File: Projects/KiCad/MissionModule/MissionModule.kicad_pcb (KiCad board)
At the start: 2 copper layers, 110 x 95 mm, 26 parts, among them J1 Conn_01x04_Pin, J2 Conn_01x04_Pin, J3 Micro_SD_Card_Det_Hirose_DM3AT, U1 ABX00012, U2 MCP2562-E-P, U3 LT1584-3.3, U4 TLP222A, U5 MCP2515-I/P, Y1 8MHz

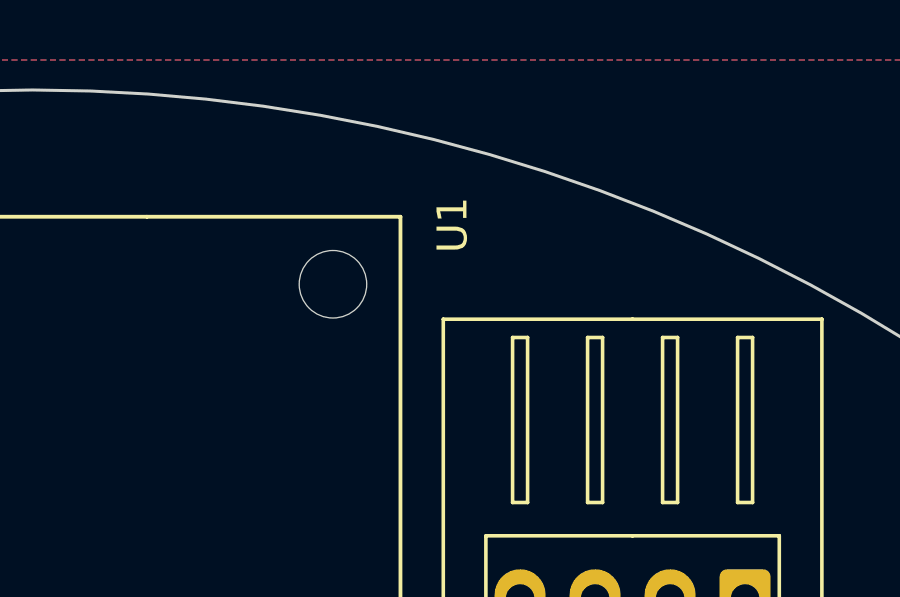
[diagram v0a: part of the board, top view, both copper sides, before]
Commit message: ADXL375のCSをGNDに接続
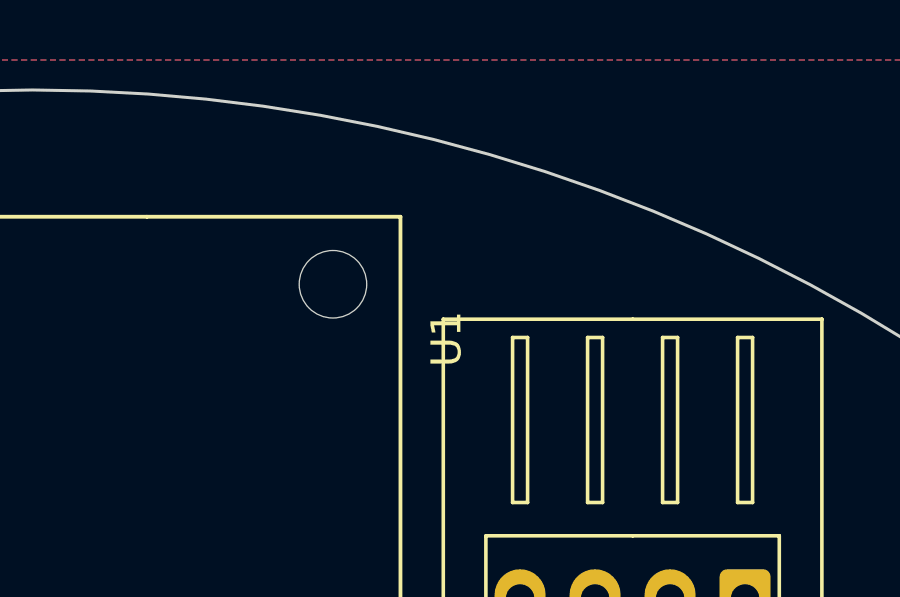
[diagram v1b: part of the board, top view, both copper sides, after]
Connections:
- U6 pad 4: unconnected-(U6-SDO/ALT_ADDRESS-Pad4) -> GND
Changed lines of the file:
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@@
   (net 51 "I2C_SCL")
   (net 52 "I2C_SDA")
-  (net 53 "unconnected-(U6-SDO{slash}ALT_ADDRESS-Pad4)")
-  (net 54 "unconnected-(U6-INT2-Pad6)")
-  (net 55 "unconnected-(U6-INT1-Pad7)")
+  (net 53 "unconnected-(U6-INT2-Pad6)")
+  (net 54 "unconnected-(U6-INT1-Pad7)")
   (footprint "Fuse:Fuse_BelFuse_0ZRE0005FF_L8.3mm_W3.8mm" (layer "F.Cu")
     (at 155.05 133.3 180)
@@
       (net 52 "I2C_SDA") (pinfunction "SDA/SDI/SDIO") (pintype "input"))
     (pad "4" thru_hole circle (at -3.73 9.04 270) (size 1.524 1.524) (drill 0.762) (layers "*.Cu" "*.Mask")
-      (net 53 "unconnected-(U6-SDO{slash}ALT_ADDRESS-Pad4)") (pinfunction "SDO/ALT_ADDRESS") (pintype "output+no_connect"))
+      (net 2 "GND") (pinfunction "SDO/ALT_ADDRESS") (pintype "output"))
     (pad "5" thru_hole circle (at -3.73 11.58 270) (size 1.524 1.524) (drill 0.762) (layers "*.Cu" "*.Mask")
       (net 5 "+3.3V") (pinfunction "~CS") (pintype "input"))
     (pad "6" thru_hole circle (at 3.89 11.58 270) (size 1.524 1.524) (drill 0.762) (layers "*.Cu" "*.Mask")
-      (net 54 "unconnected-(U6-INT2-Pad6)") (pinfunction "INT2") (pintype "output+no_connect"))
+      (net 53 "unconnected-(U6-INT2-Pad6)") (pinfunction "INT2") (pintype "output+no_connect"))
     (pad "7" thru_hole circle (at 3.89 9.04 270) (size 1.524 1.524) (drill 0.762) (layers "*.Cu" "*.Mask")
-      (net 55 "unconnected-(U6-INT1-Pad7)") (pinfunction "INT1") (pintype "output+no_connect"))
+      (net 54 "unconnected-(U6-INT1-Pad7)") (pinfunction "INT1") (pintype "output+no_connect"))
     (pad "8" thru_hole circle (at 3.89 6.5 270) (size 1.524 1.524) (drill 0.762) (layers "*.Cu" "*.Mask")
       (net 2 "GND") (pinfunction "GND") (pintype "power_in"))
@@
     (property "Sheetname" "")
     (attr through_hole)
-    (fp_text reference "U1" (at 0.275 -26.7375 -90) (layer "F.SilkS")
+    (fp_text reference "U1" (at 4.075 -26.535 -90) (layer "F.SilkS")
         (effects (font (size 1 1) (thickness 0.15)))
     )
@@
     (pad "" np_thru_hole circle locked (at 59.25 -2.25 270) (size 2.25 2.25) (drill 2.25) (layers "*.Cu" "*.Mask"))
     (pad "1" thru_hole rect locked (at 22.1348 -2.34 270) (size 1.508 1.508) (drill 1) (layers "*.Cu" "*.Mask")
-      (net 25 "unconnected-(U1-PA03_VREFA{slash}AREF-Pad1)") (pinfunction "PA03_VREFA/AREF") (pintype "bidirectional"))
+      (net 25 "unconnected-(U1-PA03_VREFA{slash}AREF-Pad1)") (pinfunction "PA03_VREFA/AREF") (pintype "bidirectional+no_connect"))
     (pad "2" thru_hole circle locked (at 24.6748 -2.34 270) (size 1.508 1.508) (drill 1) (layers "*.Cu" "*.Mask")
-      (net 26 "unconnected-(U1-PA02_AIN0{slash}DAC0{slash}A0-Pad2)") (pinfunction "PA02_AIN0/DAC0/A0") (pintype "bidirectional"))
+      (net 26 "unconnected-(U1-PA02_AIN0{slash}DAC0{slash}A0-Pad2)") (pinfunction "PA02_AIN0/DAC0/A0") (pintype "bidirectional+no_connect"))
     (pad "3" thru_hole circle locked (at 27.2148 -2.34 270) (size 1.508 1.508) (drill 1) (layers "*.Cu" "*.Mask")
-      (net 27 "unconnected-(U1-PB02_AIN10{slash}A1-Pad3)") (pinfunction "PB02_AIN10/A1") (pintype "bidirectional"))
+      (net 27 "unconnected-(U1-PB02_AIN10{slash}A1-Pad3)") (pinfunction "PB02_AIN10/A1") (pintype "bidirectional+no_connect"))
     (pad "4" thru_hole circle locked (at 29.7548 -2.34 270) (size 1.508 1.508) (drill 1) (layers "*.Cu" "*.Mask")
-      (net 28 "unconnected-(U1-PB03_AIN11{slash}A2-Pad4)") (pinfunction "PB03_AIN11/A2") (pintype "bidirectional"))
+      (net 28 "unconnected-(U1-PB03_AIN11{slash}A2-Pad4)") (pinfunction "PB03_AIN11/A2") (pintype "bidirectional+no_connect"))
     (pad "5" thru_hole circle locked (at 32.2948 -2.34 270) (size 1.508 1.508) (drill 1) (layers "*.Cu" "*.Mask")
-      (net 29 "unconnected-(U1-PA04_AIN4{slash}A3-Pad5)") (pinfunction "PA04_AIN4/A3") (pintype "bidirectional"))
+      (net 29 "unconnected-(U1-PA04_AIN4{slash}A3-Pad5)") (pinfunction "PA04_AIN4/A3") (pintype "bidirectional+no_connect"))
     (pad "6" thru_hole circle locked (at 34.8348 -2.34 270) (size 1.508 1.508) (drill 1) (layers "*.Cu" "*.Mask")
-      (net 30 "unconnected-(U1-PA05_AIN5{slash}A4-Pad6)") (pinfunction "PA05_AIN5/A4") (pintype "bidirectional"))
+      (net 30 "unconnected-(U1-PA05_AIN5{slash}A4-Pad6)") (pinfunction "PA05_AIN5/A4") (pintype "bidirectional+no_connect"))
     (pad "7" thru_hole circle locked (at 37.3748 -2.34 270) (size 1.508 1.508) (drill 1) (layers "*.Cu" "*.Mask")
-      (net 31 "unconnected-(U1-PA06_AIN6{slash}A5-Pad7)") (pinfunction "PA06_AIN6/A5") (pintype "bidirectional"))
+      (net 31 "unconnected-(U1-PA06_AIN6{slash}A5-Pad7)") (pinfunction "PA06_AIN6/A5") (pintype "bidirectional+no_connect"))
     (pad "8" thru_hole circle locked (at 39.9148 -2.34 270) (size 1.508 1.508) (drill 1) (layers "*.Cu" "*.Mask")
-      (net 32 "unconnected-(U1-PA07_AIN7{slash}A6-Pad8)") (pinfunction "PA07_AIN7/A6") (pintype "bidirectional"))
+      (net 32 "unconnected-(U1-PA07_AIN7{slash}A6-Pad8)") (pinfunction "PA07_AIN7/A6") (pintype "bidirectional+no_connect"))
     (pad "9" thru_hole circle locked (at 42.4548 -2.34 270) (size 1.508 1.508) (drill 1) (layers "*.Cu" "*.Mask")
-      (net 33 "unconnected-(U1-PA22_TC4-W0{slash}0-Pad9)") (pinfunction "PA22_TC4-W0/0") (pintype "bidirectional"))
+      (net 33 "unconnected-(U1-PA22_TC4-W0{slash}0-Pad9)") (pinfunction "PA22_TC4-W0/0") (pintype "bidirectional+no_connect"))
     (pad "10" thru_hole circle locked (at 44.9948 -2.34 270) (size 1.508 1.508) (drill 1) (layers "*.Cu" "*.Mask")
-      (net 34 "unconnected-(U1-PA23_TC4-W1{slash}1-Pad10)") (pinfunction "PA23_TC4-W1/1") (pintype "bidirectional"))
+      (net 34 "unconnected-(U1-PA23_TC4-W1{slash}1-Pad10)") (pinfunction "PA23_TC4-W1/1") (pintype "bidirectional+no_connect"))
     (pad "11" thru_hole circle locked (at 47.5348 -2.34 270) (size 1.508 1.508) (drill 1) (layers "*.Cu" "*.Mask")
-      (net 35 "unconnected-(U1-PA10_TCC0-W2{slash}~2-Pad11)") (pinfunction "PA10_TCC0-W2/~2") (pintype "bidirectional"))
+      (net 35 "unconnected-(U1-PA10_TCC0-W2{slash}~2-Pad11)") (pinfunction "PA10_TCC0-W2/~2") (pintype "bidirectional+no_connect"))
     (pad "12" thru_hole circle locked (at 50.0748 -2.34 270) (size 1.508 1.508) (drill 1) (layers "*.Cu" "*.Mask")
-      (net 36 "unconnected-(U1-PA11_TCC0-W3{slash}~3-Pad12)") (pinfunction "PA11_TCC0-W3/~3") (pintype "bidirectional"))
+      (net 36 "unconnected-(U1-PA11_TCC0-W3{slash}~3-Pad12)") (pinfunction "PA11_TCC0-W3/~3") (pintype "bidirectional+no_connect"))
     (pad "13" thru_hole circle locked (at 52.6148 -2.34 270) (size 1.508 1.508) (drill 1) (layers "*.Cu" "*.Mask")
-      (net 37 "unconnected-(U1-PB10_TCC0-W4{slash}~4-Pad13)") (pinfunction "PB10_TCC0-W4/~4") (pintype "bidirectional"))
+      (net 37 "unconnected-(U1-PB10_TCC0-W4{slash}~4-Pad13)") (pinfunction "PB10_TCC0-W4/~4") (pintype "bidirectional+no_connect"))
     (pad "14" thru_hole circle locked (at 55.1548 -2.34 270) (size 1.508 1.508) (drill 1) (layers "*.Cu" "*.Mask")
       (net 23 "MEMORY_POWER_CONTROL") (pinfunction "PB11_TCC0-W5/~5") (pintype "bidirectional"))
@@
       (net 51 "I2C_SCL") (pinfunction "PA09_S0_I2C_SCL") (pintype "bidirectional"))
     (pad "22" thru_hole circle locked (at 37.3748 -22.66 270) (size 1.508 1.508) (drill 1) (layers "*.Cu" "*.Mask")
-      (net 38 "unconnected-(U1-PB23_S5_RX-Pad22)") (pinfunction "PB23_S5_RX") (pintype "bidirectional"))
+      (net 38 "unconnected-(U1-PB23_S5_RX-Pad22)") (pinfunction "PB23_S5_RX") (pintype "bidirectional+no_connect"))
     (pad "23" thru_hole circle locked (at 34.8348 -22.66 270) (size 1.508 1.508) (drill 1) (layers "*.Cu" "*.Mask")
-      (net 39 "unconnected-(U1-PB22_S5_TX-Pad23)") (pinfunction "PB22_S5_TX") (pintype "bidirectional"))
+      (net 39 "unconnected-(U1-PB22_S5_TX-Pad23)") (pinfunction "PB22_S5_TX") (pintype "bidirectional+no_connect"))
     (pad "24" thru_hole circle locked (at 32.2948 -22.66 270) (size 1.508 1.508) (drill 1) (layers "*.Cu" "*.Mask")
-      (net 40 "unconnected-(U1-RESET-Pad24)") (pinfunction "RESET") (pintype "input"))
+      (net 40 "unconnected-(U1-RESET-Pad24)") (pinfunction "RESET") (pintype "input+no_connect"))
     (pad "25" thru_hole circle locked (at 29.7548 -22.66 270) (size 1.508 1.508) (drill 1) (layers "*.Cu" "*.Mask")
-      (net 41 "unconnected-(U1-GND-Pad25)") (pinfunction "GND") (pintype "power_in"))
+      (net 41 "unconnected-(U1-GND-Pad25)") (pinfunction "GND") (pintype "power_in+no_connect"))
     (pad "26" thru_hole circle locked (at 27.2148 -22.66 270) (size 1.508 1.508) (drill 1) (layers "*.Cu" "*.Mask")
       (net 5 "+3.3V") (pinfunction "+3V3") (pintype "power_in"))
@@
       (net 3 "+5V") (pinfunction "VIN") (pintype "power_in"))
     (pad "28" thru_hole circle locked (at 22.1348 -22.66 270) (size 1.508 1.508) (drill 1) (layers "*.Cu" "*.Mask")
-      (net 42 "unconnected-(U1-+5V-Pad28)") (pinfunction "+5V") (pintype "power_in"))
+      (net 42 "unconnected-(U1-+5V-Pad28)") (pinfunction "+5V") (pintype "power_in+no_connect"))
   )
   (footprint "MountingHole:MountingHole_4.5mm" locked (layer "F.Cu")

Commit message: 全モジュールのkicadを一通り作った
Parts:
- removed the C4 at (167.5, 123.5)
- removed the U3 at (170.0, 127.5)
- added D2: LED, LED_SMD:LED_1206_3216Metric_Pad1.42x1.75mm_HandSolder, F.Cu at (196.0, 110.0)
- added D3: LED, LED_SMD:LED_1206_3216Metric_Pad1.42x1.75mm_HandSolder, F.Cu at (196.0, 115.0)
- added D4: LED, LED_SMD:LED_1206_3216Metric_Pad1.42x1.75mm_HandSolder, F.Cu at (126.5, 133.0)
- added D5: LED, LED_SMD:LED_1206_3216Metric_Pad1.42x1.75mm_HandSolder, F.Cu at (147.5, 131.5)
- added D6: LED, LED_SMD:LED_1206_3216Metric_Pad1.42x1.75mm_HandSolder, F.Cu at (147.5, 137.5)
- added R10: 100Ω, Resistor_SMD:R_0805_2012Metric_Pad1.20x1.40mm_HandSolder, F.Cu at (190.5, 115.0)
- added R11: 100Ω, Resistor_SMD:R_0805_2012Metric_Pad1.20x1.40mm_HandSolder, F.Cu at (126.5, 127.5)
- added R12: 100Ω, Resistor_SMD:R_0805_2012Metric_Pad1.20x1.40mm_HandSolder, F.Cu at (151.0, 131.5)
- added R13: 1kΩ, Resistor_SMD:R_0805_2012Metric_Pad1.20x1.40mm_HandSolder, F.Cu at (151.0, 137.5)
- added R2: 10kΩ, Resistor_SMD:R_0805_2012Metric_Pad1.20x1.40mm_HandSolder, F.Cu at (172.5, 118.0)
- added R3: 4.7kΩ, Resistor_SMD:R_0805_2012Metric_Pad1.20x1.40mm_HandSolder, F.Cu at (147.0, 124.5)
- added R6: 2kΩ, Resistor_SMD:R_0805_2012Metric_Pad1.20x1.40mm_HandSolder, F.Cu at (186.5, 77.0)
- added R7: 4.7kΩ, Resistor_SMD:R_0805_2012Metric_Pad1.20x1.40mm_HandSolder, F.Cu at (115.2, 113.5)
- added R8: 4.7kΩ, Resistor_SMD:R_0805_2012Metric_Pad1.20x1.40mm_HandSolder, F.Cu at (100.2, 113.0)
- added R9: 100Ω, Resistor_SMD:R_0805_2012Metric_Pad1.20x1.40mm_HandSolder, F.Cu at (190.5, 110.0)
- added SW1: SW_Push, Button_Switch_THT:SW_PUSH_6mm, F.Cu at (114.5, 93.5)
- added SW2: SW_Push, Button_Switch_THT:SW_PUSH_6mm, F.Cu at (114.5, 84.5)
- added U6: MB85RS2MT, Package_DIP:DIP-8_W7.62mm, F.Cu at (116.2, 110.8)
- added U7: MB85RS2MT, Package_DIP:DIP-8_W7.62mm, F.Cu at (101.2, 110.3)
- C3: value 0.1μF -> 470μF; footprint Capacitor_SMD:C_0805_2012Metric_Pad1.18x1.45mm_HandSolder -> Capacitor_THT:CP_Radial_D10.0mm_P3.50mm
- D1: value 1N4148 -> LED; footprint Diode_THT:D_DO-35_SOD27_P7.62mm_Horizontal -> LED_SMD:LED_1206_3216Metric_Pad1.42x1.75mm_HandSolder
- moved D1 53.6 mm to (186.5, 73.5)
- moved F1 5.50 mm to (160.6, 133.3)
- moved R4 5.50 mm to (166.5, 133.5)
- moved R5 5.50 mm to (166.5, 139.0)
- moved U4 5.50 mm to (161.8, 140.8)
- moved U1 5.34 mm to (123.5, 123.6)
- moved C3 3.54 mm to (165.5, 126.0)
- moved C4 0.71 mm to (172.5, 120.5), turned to 180 degrees
- renumbered C5 to C4, C6 to C5, C7 to C6, R3 to R4, R4 to R5, U6 to U1, U1 to U2, U2 to U3
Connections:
- C3 pad 1: +5V -> +3.3V
- D1 pad 1: +5V -> GND
- F1 pad 1: Net-(D1-A) -> +3.3V
- J3 pad 10: unconnected-(J3-DET_A-Pad10) -> SD_CHECK
- J3 pad 9: unconnected-(J3-DET_B-Pad9) -> GND
- U2 pad 10: unconnected-(U1-PA23_TC4-W1/1-Pad10) -> CAN_SEND_STATUS
- U2 pad 11: unconnected-(U1-PA10_TCC0-W2/~2-Pad11) -> RECORD_STATUS
- U2 pad 12: unconnected-(U1-PA11_TCC0-W3/~3-Pad12) -> SD_CHECK
- U2 pad 13: unconnected-(U1-PB10_TCC0-W4/~4-Pad13) -> SD_STATUS
- U2 pad 5: unconnected-(U1-PA04_AIN4/A3-Pad5) -> DUMP_MODE
- U2 pad 6: unconnected-(U1-PA05_AIN5/A4-Pad6) -> DEBUG_MODE
- U2 pad 7: unconnected-(U1-PA06_AIN6/A5-Pad7) -> SPI_CS_FRAM1
- U2 pad 8: unconnected-(U1-PA07_AIN7/A6-Pad8) -> SPI_CS_FRAM0
- U2 pad 9: unconnected-(U1-PA22_TC4-W0/0-Pad9) -> CAN_RECEIVE_STATUS
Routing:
- net CAN_RECEIVE_STATUS: track 0.00 -> 80.5 mm, vias 0 -> 1
- net CAN_SEND_STATUS: track 0.00 -> 77.5 mm, vias 0 -> 1
- net +3.3V: track 159.2 -> 236.4 mm
- net MEMORY_POWER: track 19.9 -> 93.0 mm, vias 0 -> 3
- net SPI_CS_FRAM0: track 0.00 -> 54.8 mm, vias 0 -> 4
- net SPI_MOSI: track 61.8 -> 112.5 mm, vias 0 -> 3
- net SPI_SCLK: track 65.8 -> 113.7 mm, vias 0 -> 3
- net SPI_MISO: track 75.9 -> 119.9 mm, vias 2 -> 4
- net SPI_CS_FRAM1: track 0.00 -> 40.1 mm, vias 0 -> 2
- net SD_CHECK: track 0.00 -> 38.6 mm, vias 0 -> 1
- net +5V: track 106.8 -> 71.0 mm, vias 3 -> 1
- net RECORD_STATUS: track 0.00 -> 34.2 mm, vias 0 -> 2
- net SD_STATUS: track 0.00 -> 33.6 mm, vias 0 -> 2
- net Net-(D1-A): track 36.2 -> 3.71 mm, vias 1 -> 0
- net DEBUG_MODE: track 0.00 -> 27.4 mm
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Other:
- board text added: "Boot Selection"
- board text added: "CAN"
- board text added: "CAN-BUS TERMINATION RESISTOR (OPTIONAL)"
- board text added: "DEBUG"
- board text added: "DUMP"
- board text added: "POWER"
- board text added: "RECEIVE"
- board text added: "Recorder Power"
- board text added: "Recorder Status"
- board text added: "SD Status"
- board text added: "SEND"

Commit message: 一通り部品を選定
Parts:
- added D7: ORANGE, LED_SMD:LED_0603_1608Metric_Pad1.05x0.95mm_HandSolder, F.Cu at (127.0, 61.3)
- added D8: ORANGE, LED_SMD:LED_0603_1608Metric_Pad1.05x0.95mm_HandSolder, F.Cu at (126.9, 67.0)
- added R14: 100Ω, Resistor_SMD:R_0603_1608Metric_Pad0.98x0.95mm_HandSolder, F.Cu at (130.0, 61.4)
- added R15: 100Ω, Resistor_SMD:R_0603_1608Metric_Pad0.98x0.95mm_HandSolder, F.Cu at (130.0, 67.0)
- C3: value 470μF -> 100μF; footprint Capacitor_THT:CP_Radial_D10.0mm_P3.50mm -> Capacitor_SMD:CP_Elec_6.3x7.7
- C5, C6: footprint Capacitor_SMD:C_0805_2012Metric_Pad1.18x1.45mm_HandSolder -> Capacitor_SMD:C_0603_1608Metric_Pad1.08x0.95mm_HandSolder
- D1, D6: value LED -> RED; footprint LED_SMD:LED_1206_3216Metric_Pad1.42x1.75mm_HandSolder -> LED_SMD:LED_0603_1608Metric_Pad1.05x0.95mm_HandSolder
- D2, D3: value LED -> ORANGE; footprint LED_SMD:LED_1206_3216Metric_Pad1.42x1.75mm_HandSolder -> LED_SMD:LED_0603_1608Metric_Pad1.05x0.95mm_HandSolder
- D4, D5: value LED -> GREEN; footprint LED_SMD:LED_1206_3216Metric_Pad1.42x1.75mm_HandSolder -> LED_SMD:LED_0603_1608Metric_Pad1.05x0.95mm_HandSolder
- F1: footprint Fuse:Fuse_BelFuse_0ZRE0005FF_L8.3mm_W3.8mm -> Fuse:Fuse_1206_3216Metric_Pad1.42x1.75mm_HandSolder
- R1: value 120R1/4W -> 120Ω; footprint Resistor_SMD:R_0805_2012Metric_Pad1.20x1.40mm_HandSolder -> Resistor_SMD:R_0603_1608Metric_Pad0.98x0.95mm_HandSolder
- R10, R2, R3, R4, R5, R7, R8, R9: footprint Resistor_SMD:R_0805_2012Metric_Pad1.20x1.40mm_HandSolder -> Resistor_SMD:R_0603_1608Metric_Pad0.98x0.95mm_HandSolder
- R11, R12: value 100Ω -> 300Ω; footprint Resistor_SMD:R_0805_2012Metric_Pad1.20x1.40mm_HandSolder -> Resistor_SMD:R_0603_1608Metric_Pad0.98x0.95mm_HandSolder
- R13: value 1kΩ -> 300Ω; footprint Resistor_SMD:R_0805_2012Metric_Pad1.20x1.40mm_HandSolder -> Resistor_SMD:R_0603_1608Metric_Pad0.98x0.95mm_HandSolder
- R6: value 2kΩ -> 620Ω; footprint Resistor_SMD:R_0805_2012Metric_Pad1.20x1.40mm_HandSolder -> Resistor_SMD:R_0603_1608Metric_Pad0.98x0.95mm_HandSolder
- moved F1 2.05 mm to (158.5, 133.3)
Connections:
- U2 pad 3: unconnected-(U2-PB02_AIN10/A1-Pad3) -> LORA_SEND_STATUS
- U2 pad 4: unconnected-(U2-PB03_AIN11/A2-Pad4) -> LORA_RECEIVE_STATUS
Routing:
- net LORA_RECEIVE_STATUS: track 0.00 -> 27.1 mm
- net LORA_SEND_STATUS: track 0.00 -> 18.1 mm
- net Net-(D8-A): track 0.00 -> 3.33 mm
- net Net-(D7-A): track 0.00 -> 3.02 mm
- net +3.3V: track 236.4 -> 234.7 mm, vias 4 -> 5
- net Net-(F1-Pad2): track 7.06 -> 6.11 mm
- net Net-(D4-A): track 3.01 -> 3.62 mm
- net CAN_RECEIVE_STATUS: vias 1 -> 2
- net MEMORY_POWER_CONTROL: vias 1 -> 2
- net GND: vias 83 -> 89
- net CAN_SEND_STATUS: vias 1 -> 2
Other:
- board text added: "LORA"
